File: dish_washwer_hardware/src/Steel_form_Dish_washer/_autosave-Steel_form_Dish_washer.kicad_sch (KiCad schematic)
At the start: 58 parts, among them J1 RTD_TANK_SENSOR, J17 Conn_02x07_Odd_Even, J2 RTD_BOILER_SENSOR, J3 AC_PWR_IN, J4 MAG_DOOR_SENSOR, J5 Conn_02x03_Odd_Even, J6 Conn_01x04_Male, SW1 SW_Push, U1 ATmega2560-16AU, U13 EL817, U2 LM1117-3.3, U3 MAX31865ATP+T, U4 MAX31865ATP+T, Y1 C3E-16.000-12-1010-M

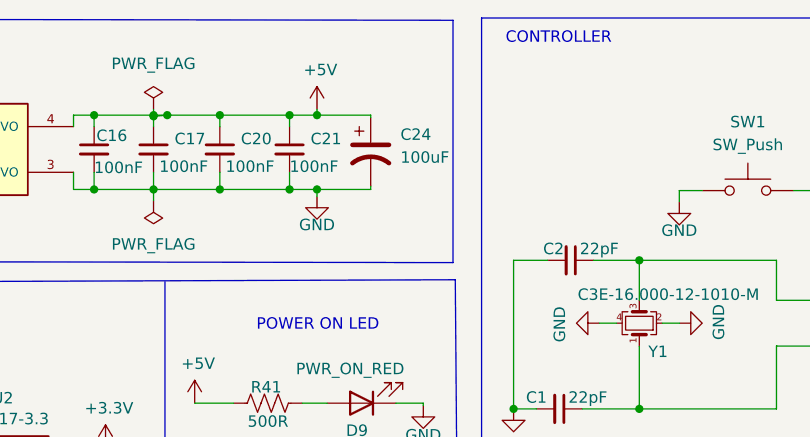
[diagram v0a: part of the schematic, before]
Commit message: updated pullup+debug+water sensor
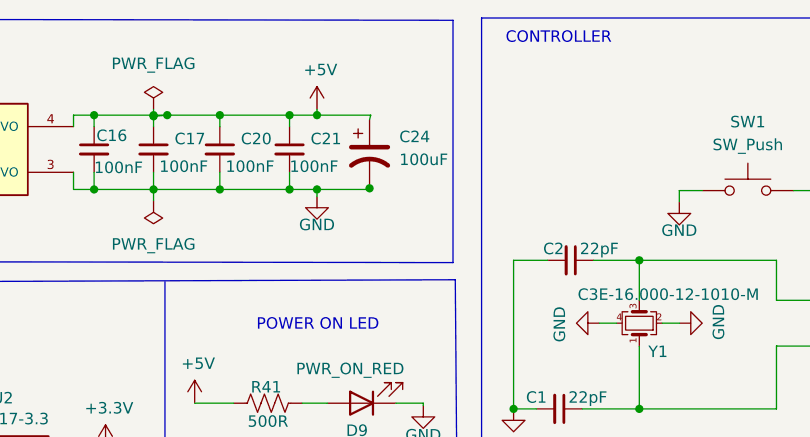
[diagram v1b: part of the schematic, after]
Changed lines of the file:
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@@
   (junction (at 32.766 117.602) (diameter 0) (color 0 0 0 0)
   )
+  (junction (at 117.983 31.496) (diameter 0) (color 0 0 0 0)
+  )
   (junction (at 86.106 212.852) (diameter 0) (color 0 0 0 0)
   )
@@
     (stroke (width 0) (type default) (color 0 0 0 0))
   )
-  (wire (pts (xy 118.11 23.622) (xy 118.11 23.368))
+  (wire (pts (xy 117.983 23.876) (xy 118.11 23.368))
     (stroke (width 0) (type default) (color 0 0 0 0))
   )
@@
     (stroke (width 0) (type default) (color 0 0 0 0))
   )
-  (wire (pts (xy 118.11 31.623) (xy 118.11 31.242))
+  (wire (pts (xy 118.11 31.623) (xy 117.983 31.496))
     (stroke (width 0) (type default) (color 0 0 0 0))
   )
@@
     (pin "2")
   )
-  (symbol (lib_id "Device:C_Polarized_US") (at 118.11 27.432 0) (unit 1)
+  (symbol (lib_id "Device:C_Polarized_US") (at 117.983 27.686 0) (unit 1)
     (in_bom yes) (on_board yes) (fields_autoplaced)
-    (property "Reference" "C24" (id 0) (at 121.412 25.5269 0)
+    (property "Reference" "C24" (id 0) (at 121.285 25.7809 0)
       (effects (font (size 1.27 1.27)) (justify left))
     )
-    (property "Value" "100uF" (id 1) (at 121.412 28.0669 0)
+    (property "Value" "100uF" (id 1) (at 121.285 28.3209 0)
       (effects (font (size 1.27 1.27)) (justify left))
     )
-    (property "Footprint" "Capacitor_SMD:CP_Elec_5x5.4" (id 2) (at 118.11 27.432 0)
+    (property "Footprint" "Capacitor_SMD:CP_Elec_5x5.4" (id 2) (at 117.983 27.686 0)
       (effects (font (size 1.27 1.27)) hide)
     )
-    (property "Datasheet" "RVT1A101M0505" (id 3) (at 118.11 27.432 0)
+    (property "Datasheet" "RVT1A101M0505" (id 3) (at 117.983 27.686 0)
       (effects (font (size 1.27 1.27)) hide)
     )
-    (property "MPN" "RVT1A101M0505" (id 4) (at 118.11 27.432 0)
+    (property "MPN" "RVT1A101M0505" (id 4) (at 117.983 27.686 0)
       (effects (font (size 0.9906 0.9906)) hide)
     )
@@
       (reference "#PWR034") (unit 1) (value "GND") (footprint "")
     )
+    (path "/00000000-0000-0000-0000-00006384df38/7a6338a7-0d7e-4021-b6fb-f86fd5ca18fa"
+      (reference "#PWR035") (unit 1) (value "+5V") (footprint "")
+    )
+    (path "/00000000-0000-0000-0000-00006384df38/33d4b003-1d60-4215-9c18-f093191346c9"
+      (reference "#PWR036") (unit 1) (value "+5V") (footprint "")
+    )
     (path "/00000000-0000-0000-0000-000061d0afb6"
       (reference "#PWR0101") (unit 1) (value "GND") (footprint "")
@@
       (reference "#PWR0175") (unit 1) (value "GND") (footprint "")
     )
-    (path "/00000000-0000-0000-0000-00006384df38/33d4b003-1d60-4215-9c18-f093191346c9"
-      (reference "#PWR?") (unit 1) (value "+5V") (footprint "")
-    )
-    (path "/00000000-0000-0000-0000-00006384df38/7a6338a7-0d7e-4021-b6fb-f86fd5ca18fa"
-      (reference "#PWR?") (unit 1) (value "+5V") (footprint "")
-    )
     (path "/bec2222d-e897-45a4-9a97-9dfbdc08b2b2"
       (reference "BZ1") (unit 1) (value "PS1240P02BT") (footprint "digikey-footprints:Piezo_Transducer_THT_PS1240P02BT")
@@
       (reference "PS1") (unit 1) (value "HLK-5M05") (footprint "greencharge-footprints:CONV_HLK-5M05")
     )
+    (path "/00000000-0000-0000-0000-00006384df38/636af961-6bdd-40dc-8c8d-f2869df59c64"
+      (reference "Q1") (unit 1) (value "DMP6023LE-13") (footprint "Package_TO_SOT_SMD:SOT-223-3_TabPin2")
+    )
     (path "/00000000-0000-0000-0000-00006384df38/00000000-0000-0000-0000-000063950bbe"
       (reference "Q3") (unit 1) (value "WST2N7002K") (footprint "Package_TO_SOT_SMD:SOT-23")
@@
       (reference "Q5") (unit 1) (value "WST2N7002K") (footprint "Package_TO_SOT_SMD:SOT-23")
     )
-    (path "/00000000-0000-0000-0000-00006384df38/636af961-6bdd-40dc-8c8d-f2869df59c64"
-      (reference "Q?") (unit 1) (value "DMP6023LE-13") (footprint "Package_TO_SOT_SMD:SOT-223-3_TabPin2")
-    )
     (path "/00000000-0000-0000-0000-000061d2b257"
       (reference "R1") (unit 1) (value "10K") (footprint "Resistor_SMD:R_0402_1005Metric")
@@
       (reference "R41") (unit 1) (value "500R") (footprint "Resistor_SMD:R_0402_1005Metric")
     )
-    (path "/00000000-0000-0000-0000-00006384df38/0d98f57d-b03b-4e47-aaf1-17eb8b4de9b8"
-      (reference "R?") (unit 1) (value "1K") (footprint "Resistor_SMD:R_0402_1005Metric")
-    )
     (path "/00000000-0000-0000-0000-00006384df38/28c2bb44-7430-47c0-aff9-c4e621c5f657"
-      (reference "R?") (unit 1) (value "1K") (footprint "Resistor_SMD:R_0402_1005Metric")
+      (reference "R42") (unit 1) (value "1K") (footprint "Resistor_SMD:R_0402_1005Metric")
     )
-    (path "/00000000-0000-0000-0000-00006384df38/73372fdf-6195-4000-b2a8-17162811f0ed"
-      (reference "R?") (unit 1) (value "1M") (footprint "Resistor_SMD:R_0402_1005Metric")
-    )
-    (path "/00000000-0000-0000-0000-00006384df38/9ba637b8-d8e7-4399-ac06-ea07dde56d6a"
-      (reference "R?") (unit 1) (value "1M") (footprint "Resistor_SMD:R_0402_1005Metric")
+    (path "/00000000-0000-0000-0000-00006384df38/0d98f57d-b03b-4e47-aaf1-17eb8b4de9b8"
+      (reference "R43") (unit 1) (value "1K") (footprint "Resistor_SMD:R_0402_1005Metric")
     )
     (path "/00000000-0000-0000-0000-00006384df38/b6fd5f4d-ac5b-4ccb-b5a2-7392a8f5b844"
-      (reference "R?") (unit 1) (value "1K") (footprint "Resistor_SMD:R_0402_1005Metric")
+      (reference "R44") (unit 1) (value "1K") (footprint "Resistor_SMD:R_0402_1005Metric")
     )
     (path "/00000000-0000-0000-0000-00006384df38/dac80e5b-60c3-4a02-8599-a161dad8d1dc"
-      (reference "R?") (unit 1) (value "1M") (footprint "Resistor_SMD:R_0402_1005Metric")
+      (reference "R45") (unit 1) (value "1M") (footprint "Resistor_SMD:R_0402_1005Metric")
+    )
+    (path "/00000000-0000-0000-0000-00006384df38/73372fdf-6195-4000-b2a8-17162811f0ed"
+      (reference "R46") (unit 1) (value "1M") (footprint "Resistor_SMD:R_0402_1005Metric")
+    )
+    (path "/00000000-0000-0000-0000-00006384df38/9ba637b8-d8e7-4399-ac06-ea07dde56d6a"
+      (reference "R47") (unit 1) (value "1M") (footprint "Resistor_SMD:R_0402_1005Metric")
     )
     (path "/00000000-0000-0000-0000-000064bca22e"
